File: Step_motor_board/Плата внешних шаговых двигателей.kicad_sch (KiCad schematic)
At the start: 37 parts, among them J1 Prog (PinHeader_2x03_P2.54mm), Q4 DTC114ECA (SOT-23), Q5 DTC114ECA (SOT-23), U1 ADM3485EARZ-REEL (SOIC-8), U2 ISO6741FDWR (SOIC-16W), U3 STM32G070RBTx (LQFP-64), U5 AM1SS-2403SJZ

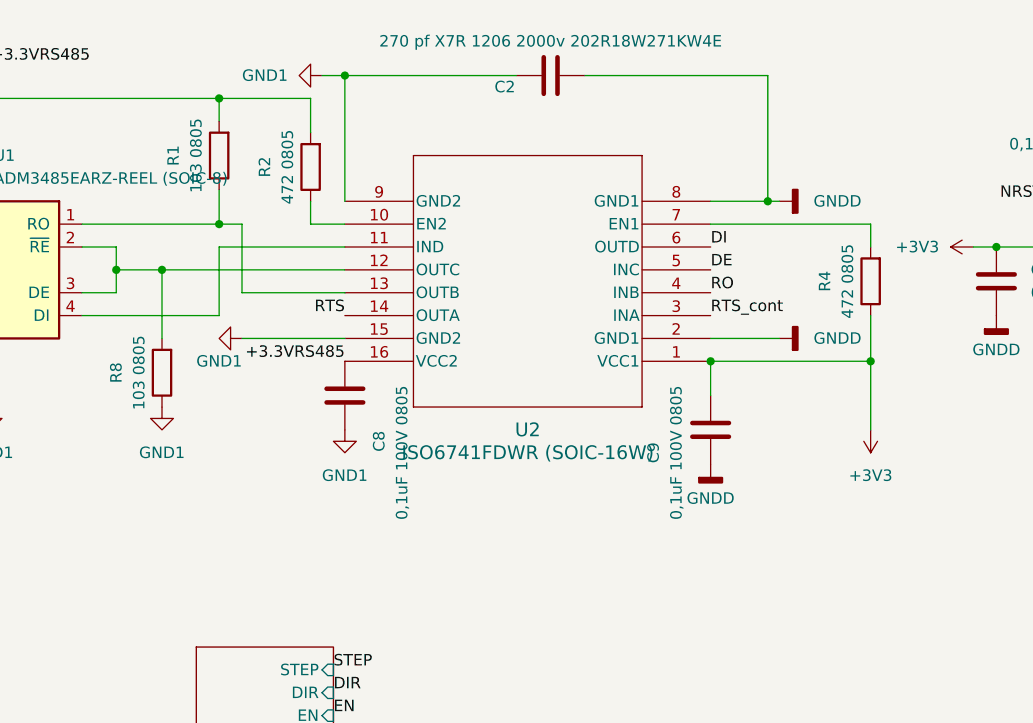
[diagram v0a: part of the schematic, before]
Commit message: Modify Digit_IN, Motherbord, Step motors
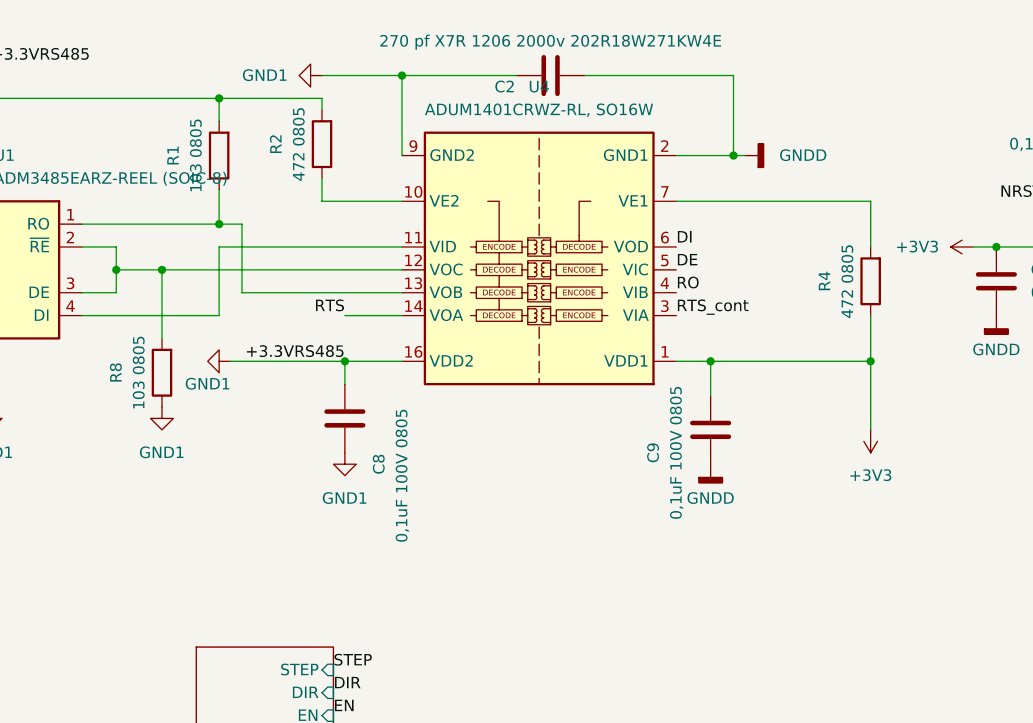
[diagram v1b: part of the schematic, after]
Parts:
- removed U2: ISO6741FDWR (SOIC-16W), PCM_Package_SO_AKL:SOIC-16W_7.5x10.3mm_P1.27mm, symbol Isolator:ISO6741FDWR
- added U4: ADUM1401CRWZ-RL, SO16W, Package_SO:SOIC-16W_7.5x10.3mm_P1.27mm, symbol Isolator:ADuM1401xRW
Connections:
- net +3.3VRS485 is gone; now on net GND1: C1.2, C5.2, C8.2, R1.2, R2.2, R3.2, RS1.1 (Pin_1), RS1.10 (Pin_10), U1.8 (VCC)
- net +3V3: now also U4.1 (VDD1)
- net DE: now also U4.5 (VIC)
- net DI: now also U4.6 (VOD)
- net GND1: now also U4.15 (GND2), U4.16 (VDD2), U4.9 (GND2)
- net GNDD: now also U4.2 (GND1), U4.8 (GND1)
- net RO: now also U4.4 (VIB)
- net RTS: now also U4.14 (VOA)
- net RTS_cont: now also U4.3 (VIA)
- net at R8.2, U1.2 (~{RE}), U1.3 (DE): now also U4.12 (VOC)
- net at R1.1, U1.1 (RO): now also U4.13 (VOB)
- net at U1.4 (DI): now also U4.11 (VID)
- net at R2.1: now also U4.10 (VE2)
- net at R4.2: now also U4.7 (VE1)
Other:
- moved on the sheet: C8, R2

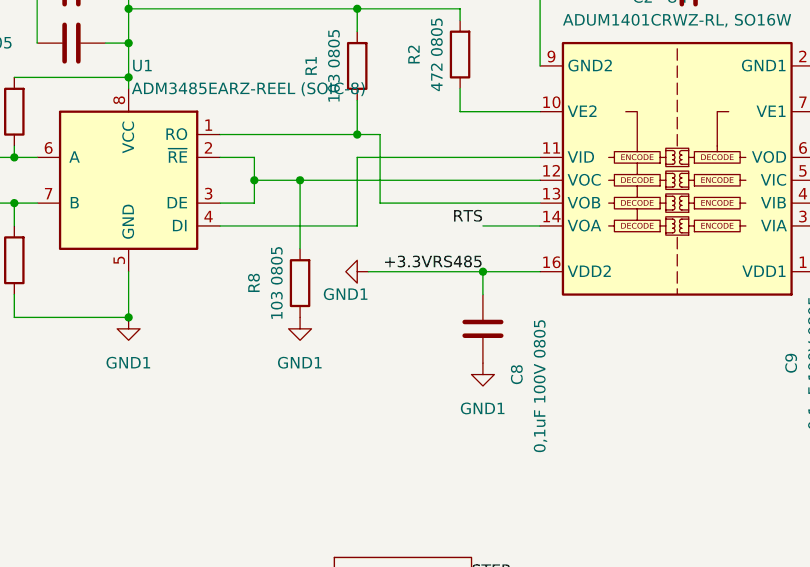
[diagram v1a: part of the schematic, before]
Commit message: Modify Digit_IN, Motherbord, Step motors, photo
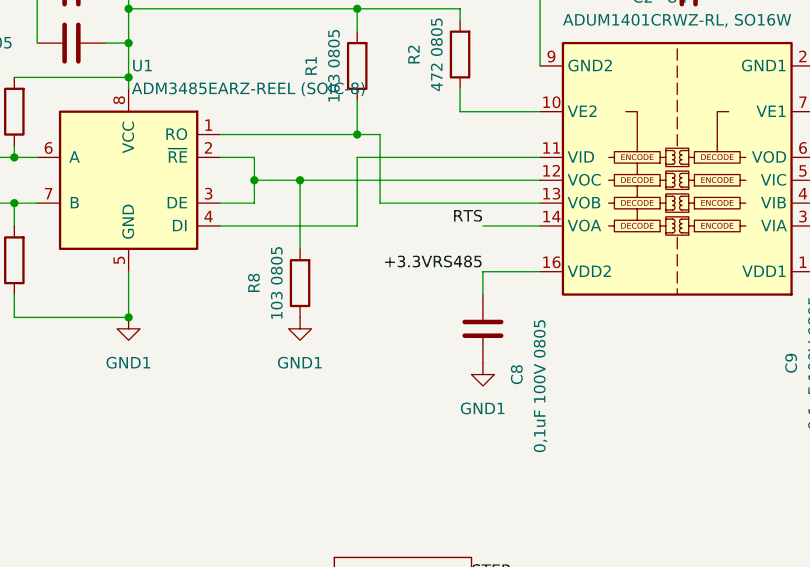
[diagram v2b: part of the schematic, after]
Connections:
- net GND1: no longer C1.2, C5.2, C8.2, R1.2, R2.2, R3.2, RS1.1 (Pin_1), RS1.10 (Pin_10), U1.8 (VCC), U4.16 (VDD2)
- new net +3.3VRS485: C1.2, C5.2, C8.2, R1.2, R2.2, R3.2, RS1.1 (Pin_1), RS1.10 (Pin_10), U1.8 (VCC), U4.16 (VDD2)
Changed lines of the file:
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@@
   (junction (at 175.26 38.1) (diameter 0) (color 0 0 0 0)
   )
-  (junction (at 102.87 50.8) (diameter 0) (color 0 0 0 0)
-  )
   (junction (at 161.29 50.8) (diameter 0) (color 0 0 0 0)
   )
@@
   )
   (wire (pts (xy 63.5 21.59) (xy 88.9 21.59))
-    (stroke (width 0) (type default))
-  )
-  (wire (pts (xy 102.87 50.8) (xy 90.17 50.8))
     (stroke (width 0) (type default))
   )
@@
         )
       )
-    )
-  )
-  (symbol (lib_id "power:GND1") (at 90.17 50.8 270) (unit 1)
-    (in_bom yes) (on_board yes) (dnp no)
-    (property "Reference" "#PWR012" (at 83.82 50.8 0)
-      (effects (font (size 1.27 1.27)) hide)
-    )
-    (property "Value" "GND1" (at 85.09 53.34 90)
-      (effects (font (size 1.27 1.27)) (justify left))
-    )
-    (property "Footprint" "" (at 90.17 50.8 0)
-      (effects (font (size 1.27 1.27)) hide)
-    )
-    (property "Datasheet" "" (at 90.17 50.8 0)
-      (effects (font (size 1.27 1.27)) hide)
-    )
-    (pin "1")
-    (instances
-      (project "Плата внешних шаговых двигателей"
-        (path "/7f8f7dc9-8c50-44ed-985c-35a6d8c67be0"
-          (reference "#PWR012") (unit 1)
-        )
-      )

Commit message: Modify StepMotor Schems and PCB1
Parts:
- added J7: DebbagUSART (PinHeader_01x02_P2.54mm), Connector_PinHeader_2.54mm:PinHeader_1x02_P2.54mm_Vertical, symbol Connector:Conn_01x02_Pin
- added J8: Debbag GPIO (PinHeader_01x02_P2.54mm), Connector_PinHeader_2.54mm:PinHeader_1x02_P2.54mm_Vertical, symbol Connector:Conn_01x02_Pin
- U5: footprint Converter_DCDC:Converter_DCDC_Murata_MEE3SxxxxSC_THT -> Converter_DCDC:Converter_DCDC_Murata_MEE1SxxxxSC_THT
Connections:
- net ALARM: now also U3.16 (PC3); no longer U3.29 (PB2)
- net DI1: now also U3.33 (PB13); no longer U3.31 (PB11)
- net DI2: now also U3.34 (PB14); no longer U3.32 (PB12)
- net DIR: now also U3.13 (PC0); no longer U3.34 (PB14)
- net EN: now also U3.14 (PC1); no longer U3.33 (PB13)
- net IN_POSITION: now also U3.17 (PA0); no longer U3.30 (PB10)
- net STEP: now also U3.15 (PC2); no longer U3.36 (PA8)
- net GPIO1: now reaches U3.25 (PC4)
- net GPIO1: now also J8.1 (Pin_1)
- net GPIO2: now reaches U3.26 (PC5)
- net GPIO2: now also J8.2 (Pin_2)
- net DI4: now reaches U3.35 (PB15)
- net UART_TX: now reaches U3.40 (PD8)
- net UART_TX: now also J7.1 (Pin_1)
- net UART_RX: now reaches U3.41 (PD9)
- net UART_RX: now also J7.2 (Pin_2)
- net at R1.1, U1.1 (RO): now also U4.11 (VID); no longer U4.13 (VOB)
- net at U1.4 (DI): now also U4.13 (VOB); no longer U4.11 (VID)
- net DE renamed DE_USART_1
- net DI renamed RX_USART_1
- net RO renamed TX_USART_1
- new net DI3: U3.36 (PA8)
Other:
- added sheet Detectors (Detectors.kicad_sch)
- sheet Stepper_Motor_Control ports: added none; removed DI1, DI2
- moved on the sheet: J1

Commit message: Modify Mian controller, stepmotor, motor 25.05.24
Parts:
- J7: value DebbagUSART (PinHeader_01x02_P2.54mm) -> DebugUSART (PinHeader_01x02_P2.54mm)
- J8: value Debbag GPIO (PinHeader_01x02_P2.54mm) -> Debug GPIO (PinHeader_01x02_P2.54mm)
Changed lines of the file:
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@@
       (effects (font (size 1.27 1.27)))
     )
-    (property "Value" "Debbag GPIO (PinHeader_01x02_P2.54mm)" (at 44.45 106.68 0)
+    (property "Value" "Debug GPIO (PinHeader_01x02_P2.54mm)" (at 44.45 106.68 0)
       (effects (font (size 1.27 1.27)))
     )
@@
       (effects (font (size 1.27 1.27)))
     )
-    (property "Value" "DebbagUSART (PinHeader_01x02_P2.54mm)" (at 44.45 90.17 0)
+    (property "Value" "DebugUSART (PinHeader_01x02_P2.54mm)" (at 44.45 90.17 0)
       (effects (font (size 1.27 1.27)))
     )

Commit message: Add DE USART 03.06.24
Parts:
- J7: value DebugUSART (PinHeader_01x02_P2.54mm) -> DebugUSART (PinHeader_01x03_P2.54mm); footprint Connector_PinHeader_2.54mm:PinHeader_1x02_P2.54mm_Vertical -> Connector_PinHeader_2.54mm:PinHeader_1x03_P2.54mm_Vertical; symbol Connector:Conn_01x02_Pin -> Connector:Conn_01x03_Pin
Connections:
- net UART_DE: now reaches U3.39 (PC7)
- net UART_DE: now also J7.3 (Pin_3)
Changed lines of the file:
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@@
     (effects (font (size 1.27 1.27)) (justify left bottom))
+  )
+  (label "UART_DE" (at 198.12 93.98 180) (fields_autoplaced)
+    (effects (font (size 1.27 1.27)) (justify right bottom))
   )
   (label "DE_USART_1" (at 228.6 63.5 0) (fields_autoplaced)
@@
     (effects (font (size 1.27 1.27)) (justify right bottom))
   )
-  (label "UART_TX" (at 48.26 93.98 0) (fields_autoplaced)
+  (label "UART_TX" (at 48.26 91.44 0) (fields_autoplaced)
     (effects (font (size 1.27 1.27)) (justify left bottom))
   )
@@
     (effects (font (size 1.27 1.27)) (justify right bottom))
   )
-  (label "UART_RX" (at 48.26 96.52 0) (fields_autoplaced)
+  (label "UART_RX" (at 48.26 93.98 0) (fields_autoplaced)
     (effects (font (size 1.27 1.27)) (justify left bottom))
   )
@@
   )
   (label "DI2" (at 228.6 111.76 0) (fields_autoplaced)
+    (effects (font (size 1.27 1.27)) (justify left bottom))
+  )
+  (label "UART_DE" (at 48.26 96.52 0) (fields_autoplaced)
     (effects (font (size 1.27 1.27)) (justify left bottom))
   )
@@
     )
   )
-  (symbol (lib_id "Connector:Conn_01x02_Pin") (at 43.18 93.98 0) (unit 1)
+  (symbol (lib_id "Connector:Conn_01x03_Pin") (at 43.18 93.98 0) (unit 1)
     (in_bom yes) (on_board yes) (dnp no)
     (property "Reference" "J7" (at 44.45 87.63 0)
       (effects (font (size 1.27 1.27)))
     )
-    (property "Value" "DebugUSART (PinHeader_01x02_P2.54mm)" (at 44.45 90.17 0)
-      (effects (font (size 1.27 1.27)))
-    )
-    (property "Footprint" "Connector_PinHeader_2.54mm:PinHeader_1x02_P2.54mm_Vertical" (at 43.18 93.98 0)
+    (property "Value" "DebugUSART (PinHeader_01x03_P2.54mm)" (at 44.45 83.82 0)
+      (effects (font (size 1.27 1.27)))
+    )
+    (property "Footprint" "Connector_PinHeader_2.54mm:PinHeader_1x03_P2.54mm_Vertical" (at 43.18 93.98 0)
       (effects (font (size 1.27 1.27)) hide)
     )
@@
     (pin "1")
     (pin "2")
-    (instances
-      (project "Плата внешних шаговых двигателей"
+    (pin "3")
+    (instances
+      (project "Плата внешних шаговых двигателей"

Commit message: Change ISOLATOR 03.06.24
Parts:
- removed U4: ADUM1401CRWZ-RL, SO16W, Package_SO:SOIC-16W_7.5x10.3mm_P1.27mm, symbol Isolator:ADuM1401xRW
- added U9: π141M3x, Package_SO:SOIC-16_3.9x9.9mm_P1.27mm, symbol Isolator:π141M3x
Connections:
- net +3.3VRS485: now also U9.16 (VDD2)
- net +3V3: now also U9.1 (VDD1)
- net DE_USART_1: now also U9.5 (VIC)
- net GND1: now also U9.15 (GND2), U9.9 (GND2)
- net GNDD: now also U9.2 (GND1), U9.8 (GND1)
- net RTS: now also U9.14 (VOA)
- net RTS_cont: now also U9.3 (VIA)
- net RX_USART_1: now also U9.6 (VOD)
- net TX_USART_1: now also U9.4 (VIB)
- net at R8.2, U1.2 (~{RE}), U1.3 (DE): now also U9.12 (VOC)
- net at R1.1, U1.1 (RO): now also U9.11 (VID)
- net at U1.4 (DI): now also U9.13 (VOB)
- net at R4.2: now also U9.7 (VE1)
- net at R2.1: now also U9.10 (VE2)
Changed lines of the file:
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@@
-    )
-  )
-  (symbol (lib_id "Isolator:ADuM1401xRW") (at 124.46 38.1 180) (unit 1)
-    (in_bom yes) (on_board yes) (dnp no)
-    (property "Reference" "U4" (at 124.46 20.32 0)
-      (effects (font (size 1.27 1.27)))
-    )
-    (property "Value" "ADUM1401CRWZ-RL, SO16W" (at 124.46 22.86 0)
-      (effects (font (size 1.27 1.27)))
-    )
-    (property "Footprint" "Package_SO:SOIC-16W_7.5x10.3mm_P1.27mm" (at 124.46 23.495 0)
-      (effects (font (size 1.27 1.27)) hide)
-    )
-    (property "Datasheet" "https://www.analog.com/media/en/technical-documentation/data-sheets/ADUM1400_1401_1402.pdf" (at 144.78 38.1 0)
-      (effects (font (size 1.27 1.27)) hide)
-    )
-    (pin "10")
-    (pin "9")
-    (pin "4")
-    (pin "8")
-    (pin "1")
-    (pin "13")
-    (pin "2")
-    (pin "11")
-    (pin "7")
-    (pin "5")
-    (pin "12")
-    (pin "3")
-    (pin "6")
-    (pin "14")
-    (pin "16")
-    (pin "15")
-    (instances
-      (project "Плата внешних шаговых двигателей"
-        (path "/7f8f7dc9-8c50-44ed-985c-35a6d8c67be0/0d239b34-7914-40bc-9b83-7e562c30defe"
-          (reference "U4") (unit 1)
-        )
-        (path "/7f8f7dc9-8c50-44ed-985c-35a6d8c67be0"
-          (reference "U2") (unit 1)
-        )
-      )
     )
   )
@@
         )
       )
+    )
+  )
+  (symbol (lib_id "Isolator:π141M3x") (at 124.46 38.1 180) (unit 1)
+    (in_bom yes) (on_board yes) (dnp no)
+    (property "Reference" "U9" (at 124.46 58.42 0)
+      (effects (font (size 1.27 1.27)))
+    )
+    (property "Value" "π141M3x" (at 124.46 55.88 0)
+      (effects (font (size 1.27 1.27)))
+    )
+    (property "Footprint" "Package_SO:SOIC-16_3.9x9.9mm_P1.27mm" (at 124.46 23.495 0)
+      (effects (font (size 1.27 1.27)) hide)
+    )
+    (property "Datasheet" "https://wmsc.lcsc.com/wmsc/upload/file/pdf/v2/lcsc/2001082007_2Pai-Semi--141M30_C471604.pdf" (at 144.78 38.1 0)
+      (effects (font (size 1.27 1.27)) hide)
+    )
+    (pin "10")
+    (pin "14")
+    (pin "4")
+    (pin "16")
+    (pin "9")
+    (pin "6")
+    (pin "3")
+    (pin "7")
+    (pin "1")
+    (pin "15")
+    (pin "13")
+    (pin "11")
+    (pin "8")
+    (pin "2")
+    (pin "5")
+    (pin "12")
+    (instances
+      (project "Плата внешних шаговых двигателей"
+        (path "/7f8f7dc9-8c50-44ed-985c-35a6d8c67be0"
+          (reference "U9") (unit 1)
+        )
+      )

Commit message: pcb and schems step 05.06.24
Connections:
- net UART_DE: now also J7.1 (Pin_1); no longer J7.3 (Pin_3)
- net UART_RX: now also J7.3 (Pin_3); no longer J7.2 (Pin_2)
- net UART_TX: now also J7.2 (Pin_2); no longer J7.1 (Pin_1)
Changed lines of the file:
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@@
   (junction (at 63.5 19.05) (diameter 0) (color 0 0 0 0)
   )
+  (junction (at 39.37 175.26) (diameter 0) (color 0 0 0 0)
+  )
   (junction (at 88.9 35.56) (diameter 0) (color 0 0 0 0)
   )
@@
   (junction (at 82.55 40.64) (diameter 0) (color 0 0 0 0)
   )
-  (junction (at 34.29 175.26) (diameter 0) (color 0 0 0 0)
-  )
   (junction (at 63.5 29.21) (diameter 0) (color 0 0 0 0)
   )
@@
     (stroke (width 0) (type default))
   )
-  (wire (pts (xy 34.29 177.8) (xy 34.29 175.26))
+  (wire (pts (xy 39.37 177.8) (xy 39.37 175.26))
     (stroke (width 0) (type default))
   )
@@
     (stroke (width 0) (type default))
   )
+  (wire (pts (xy 39.37 175.26) (xy 44.45 175.26))
+    (stroke (width 0) (type default))
+  )
   (wire (pts (xy 266.7 81.28) (xy 273.05 81.28))
     (stroke (width 0) (type default))
@@
     (stroke (width 0) (type default))
   )
-  (wire (pts (xy 31.75 177.8) (xy 34.29 177.8))
+  (wire (pts (xy 31.75 177.8) (xy 39.37 177.8))
     (stroke (width 0) (type default))
   )
@@
     (stroke (width 0) (type default))
   )
+  (wire (pts (xy 31.75 175.26) (xy 39.37 175.26))
+    (stroke (width 0) (type default))
+  )
   (wire (pts (xy 240.03 83.82) (xy 254 83.82))
     (stroke (width 0) (type default))
@@
     (stroke (width 0) (type default))
   )
-  (wire (pts (xy 34.29 175.26) (xy 44.45 175.26))
-    (stroke (width 0) (type default))
-  )
   (wire (pts (xy 251.46 53.34) (xy 256.54 53.34))
     (stroke (width 0) (type default))
@@
     (stroke (width 0) (type default))
   )
-  (wire (pts (xy 31.75 175.26) (xy 34.29 175.26))
-    (stroke (width 0) (type default))
-  )
   (wire (pts (xy 139.7 50.8) (xy 143.51 50.8))
     (stroke (width 0) (type default))
@@
     (effects (font (size 1.27 1.27)) (justify right bottom))
   )
-  (label "UART_TX" (at 48.26 91.44 0) (fields_autoplaced)
+  (label "UART_TX" (at 48.26 93.98 0) (fields_autoplaced)
     (effects (font (size 1.27 1.27)) (justify left bottom))
   )
@@
     (effects (font (size 1.27 1.27)) (justify right bottom))
   )
-  (label "UART_RX" (at 48.26 93.98 0) (fields_autoplaced)
+  (label "UART_RX" (at 48.26 96.52 0) (fields_autoplaced)
     (effects (font (size 1.27 1.27)) (justify left bottom))
   )
@@
     (effects (font (size 1.27 1.27)) (justify left bottom))
   )
-  (label "UART_DE" (at 48.26 96.52 0) (fields_autoplaced)
-    (effects (font (size 1.27 1.27)) (justify left bottom))
-  )
+  (label "UART_DE" (at 48.26 91.44 0) (fields_autoplaced)
+    (effects (font (size 1.27 1.27)) (justify left bottom))
+  )

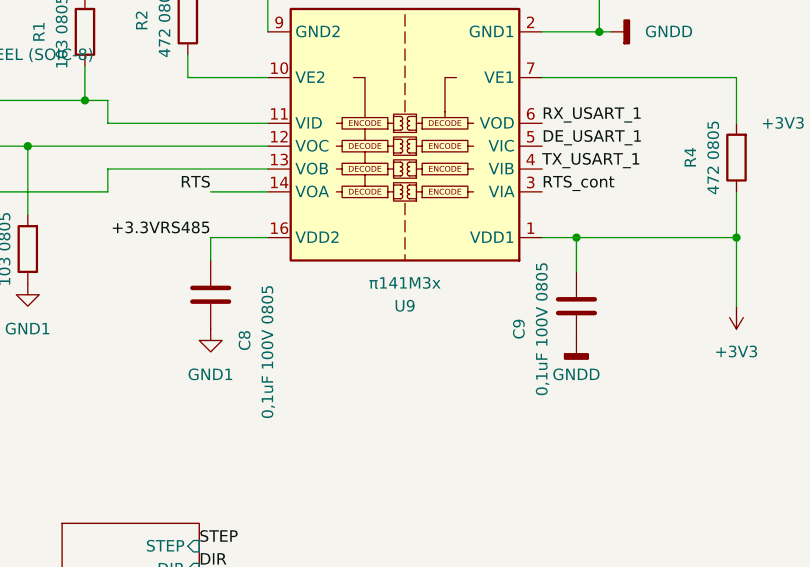
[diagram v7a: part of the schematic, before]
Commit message: stepmotor add r41 10.06.24
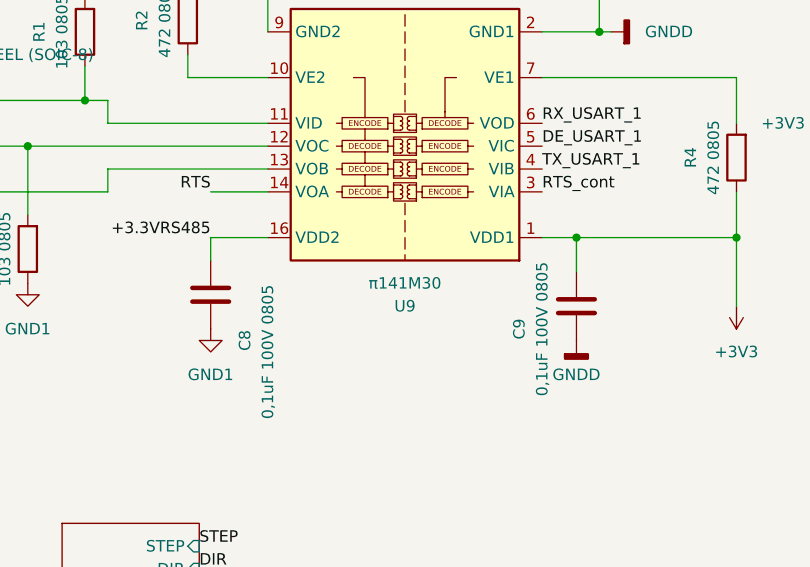
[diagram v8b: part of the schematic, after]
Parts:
- U9: value π141M3x -> π141M30
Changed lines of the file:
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@@
       (effects (font (size 1.27 1.27)))
     )
-    (property "Value" "π141M3x" (at 124.46 55.88 0)
+    (property "Value" "π141M30" (at 124.46 55.88 0)
       (effects (font (size 1.27 1.27)))
     )
